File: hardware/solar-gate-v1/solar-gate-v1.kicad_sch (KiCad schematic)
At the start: 17 parts, among them J1 SOLAR_PANEL_IN, J2 CHG_OUT, J4 TELEM_OUT, Q1 AO3401, U1 TLV3401

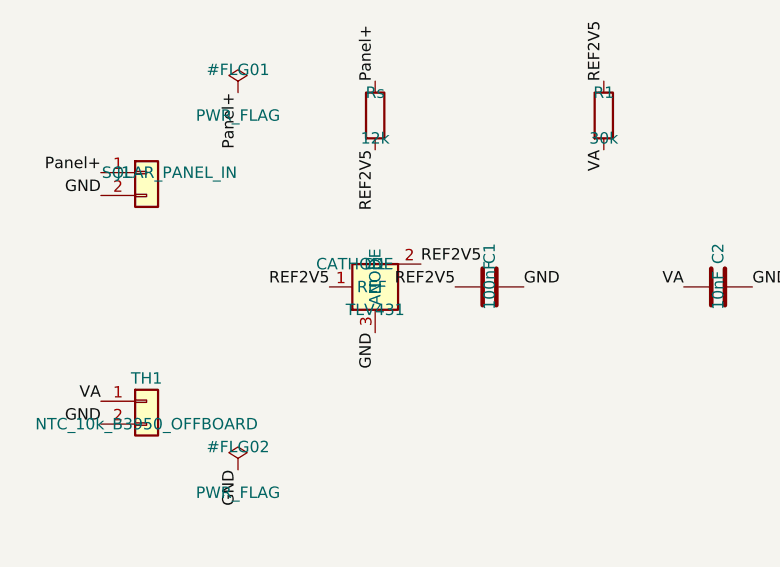
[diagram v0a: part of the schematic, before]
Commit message: 0043: swap D1 TLV431 -> TL431 (SOT-23 DBZ pinout, 2.5 V)
D1 replaced with a project-local TL431 symbol imported from KiCad's
Reference_Voltage:TL431DBZ (DBZ pinout: 1=K, 2=REF, 3=A). REF and K are both
on REF2V5 by design, so net-per-pad is unchanged (pad1 REF2V5, pad2 REF2V5,
pad3 GND) and the board file is untouched and byte-identical to the 0039 tip.

- solar-gate-v1.kicad_sym: TL431 added (SOT-23, TI SLVS543S datasheet link)
- solar-gate-v1.kicad_sch: D1 = solar-gate-v1:TL431, 3 pin labels moved to the
  new pin coordinates
- ERC 0 errors / 0 warnings; DRC re-run: 2 errors / 0 warnings (unchanged
  router stubs on net VA)
- BOM: D1 line now TL431
- sym-lib-table:  instead of an absolute checkout path (the absolute
  path made ERC fail with 'symbol library not found' from any other checkout)
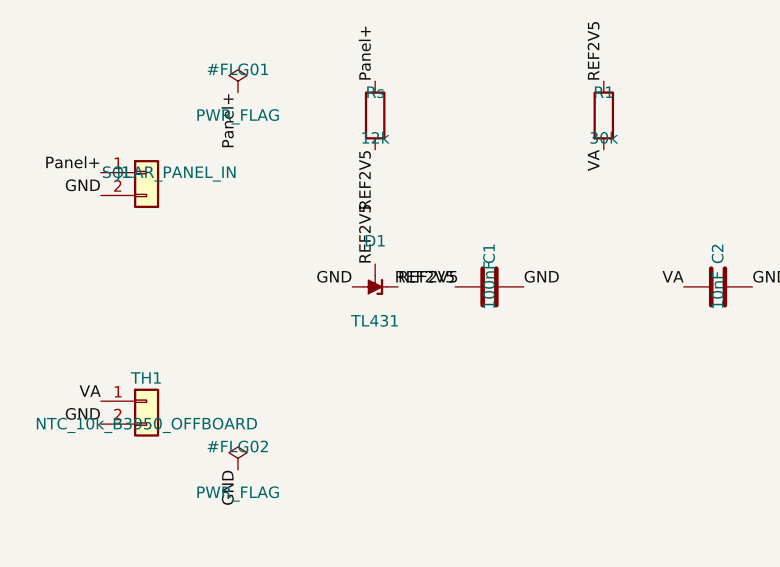
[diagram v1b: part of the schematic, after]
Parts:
- removed D1: TLV431, Package_TO_SOT_SMD:SOT-23, symbol solar-gate-v1:TLV431
- added D1: TL431, Package_TO_SOT_SMD:SOT-23, symbol solar-gate-v1:TL431
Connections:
- net GND: now also D1.3 (A)
- net REF2V5: now also D1.1 (K), D1.2 (REF)
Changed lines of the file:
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@@
-	)
-	(symbol
-		(lib_id "solar-gate-v1:TLV431")
-		(at 76.2 63.5 0)
-		(unit 1)
-		(body_style 1)
-		(exclude_from_sim no)
-		(in_bom yes)
-		(on_board yes)
-		(in_pos_files yes)
-		(dnp no)
-		(property "Reference" "D1"
-			(at 76.2 60.96 0)
-			(show_name no)
-			(do_not_autoplace no)
-			(effects
-				(font
-					(size 1.27 1.27)
-				)
-			)
-		)
-		(property "Value" "TLV431"
-			(at 76.2 66.04 0)
-			(show_name no)
-			(do_not_autoplace no)
-			(effects
-				(font
-					(size 1.27 1.27)
-				)
-			)
-		)
-		(property "Footprint" "Package_TO_SOT_SMD:SOT-23"
-			(at 76.2 58.42 0)
-			(hide yes)
-			(show_name no)
-			(do_not_autoplace no)
-			(effects
-				(font
-					(size 1.27 1.27)
-				)
-			)
-		)
-		(property "Datasheet" ""
-			(at 76.2 55.88 0)
-			(hide yes)
-			(show_name no)
-			(do_not_autoplace no)
-			(effects
-				(font
-					(size 1.27 1.27)
-				)
-			)
-		)
-		(property "Description" "Low-voltage adjustable precision shunt regulator 1.24V, SOT-23-3"
-			(at 76.2 53.34 0)
-			(hide yes)
-			(show_name no)
-			(do_not_autoplace no)
-			(effects
-				(font
-					(size 1.27 1.27)
-				)
-			)
-		)
-		(pin "1"
-		)
-		(pin "2"
-		)
-		(pin "3"
-		)
-		(instances
-			(project "solar-gate-v1"
-				(path "/0c31090d-ef25-44de-977d-fcaf1aa2b30e"
-					(reference "D1")
-					(unit 1)
-				)
-			)
-		)
 	)
 	(symbol
@@
 	)
 	(label "GND"
-		(at 76.2 68.58 270)
-		(effects
-			(font
-				(size 1.27 1.27)
-			)
-			(justify right bottom)
-		)
-	)
-	(label "GND"
 		(at 45.72 78.74000000000001 180)
 		(effects
@@
 	)
 	(label "REF2V5"
-		(at 81.28 60.96 0)
-		(effects
-			(font
-				(size 1.27 1.27)
-			)
-			(justify left bottom)
-		)
-	)
-	(label "REF2V5"
-		(at 71.12 63.5 180)
-		(effects
-			(font
-				(size 1.27 1.27)
-			)
-			(justify right bottom)
-		)
-	)
-	(label "REF2V5"
 		(at 101.6 40.64 90)
 		(effects
@@
 		(effects
 			(font
+				(size 1.27 1.27)
+			)
+			(justify right bottom)
+		)
+	)
+	(symbol
+		(lib_id "solar-gate-v1:TL431")
+		(at 76.2 63.5 0)
+		(unit 1)
+		(body_style 1)
+		(exclude_from_sim no)
+		(in_bom yes)
+		(on_board yes)
+		(in_pos_files yes)
+		(dnp no)
+		(property "Reference" "D1"
+			(at 76.2 58.42 0)
+			(show_name no)
+			(do_not_autoplace no)
+			(effects
+				(font
+					(size 1.27 1.27)
+				)
+			)
+		)
+		(property "Value" "TL431"
+			(at 76.2 67.31 0)
+			(show_name no)
+			(do_not_autoplace no)
+			(effects
+				(font
+					(size 1.27 1.27)
+				)
+			)
+		)
+		(property "Footprint" "Package_TO_SOT_SMD:SOT-23"
+			(at 76.2 58.674 0)
+			(hide yes)
+			(show_name no)
+			(do_not_autoplace no)
+			(effects
+				(font
+					(size 1.27 1.27)
+					(italic yes)
+				)
+			)
+		)
+		(property "Datasheet" "http://www.ti.com/lit/ds/symlink/tl431.pdf"
+			(at 77.978 54.356 0)
+			(hide yes)
+			(show_name no)
+			(do_not_autoplace no)
+			(effects
+				(font
+					(size 1.27 1.27)
+					(italic yes)
+				)
+			)
+		)
+		(property "Description" "2.5 V adjustable precision shunt regulator, SOT-23-3 (DBZ pinout: 1=K, 2=REF, 3=A)"
+			(at 76.2 56.388 0)
+			(hide yes)
+			(show_name no)
+			(do_not_autoplace no)
+			(effects
+				(font
+					(size 1.27 1.27)
+				)
+			)
+		)
+		(pin "1"
+		)
+		(pin "2"
+		)
+		(pin "3"
+		)
+		(instances
+			(project "solar-gate-v1"
+				(path "/0c31090d-ef25-44de-977d-fcaf1aa2b30e"
+					(reference "D1")
+					(unit 1)
+				)
+			)
+		)
+	)
+	(label "REF2V5"
+		(at 78.74000000000001 63.5 0)
+		(effects
+			(font
+				(size 1.27 1.27)
+			)
+			(justify left bottom)
+		)
+	)
+	(label "REF2V5"
+		(at 76.2 60.96 90)
+		(effects
+			(font
+				(size 1.27 1.27)
+			)
+			(justify left bottom)
+		)
+	)
+	(label "GND"
+		(at 73.66 63.5 180)
+		(effects
+			(font
